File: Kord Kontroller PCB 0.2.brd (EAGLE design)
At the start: 242.5 x 100 mm, 190 parts, among them IC2 74HCT1G125DBV, J1 MIDIOUTB, J2 MIDIOUTA, J3 FTSH-105-01-L-DV-KJ, SW2 SPST_TACT-KMR2, U1 AP2112K-3.3, U2 ATSAMD51J19A-AUT, Y1 ECS-.327-12.5-17X-TR

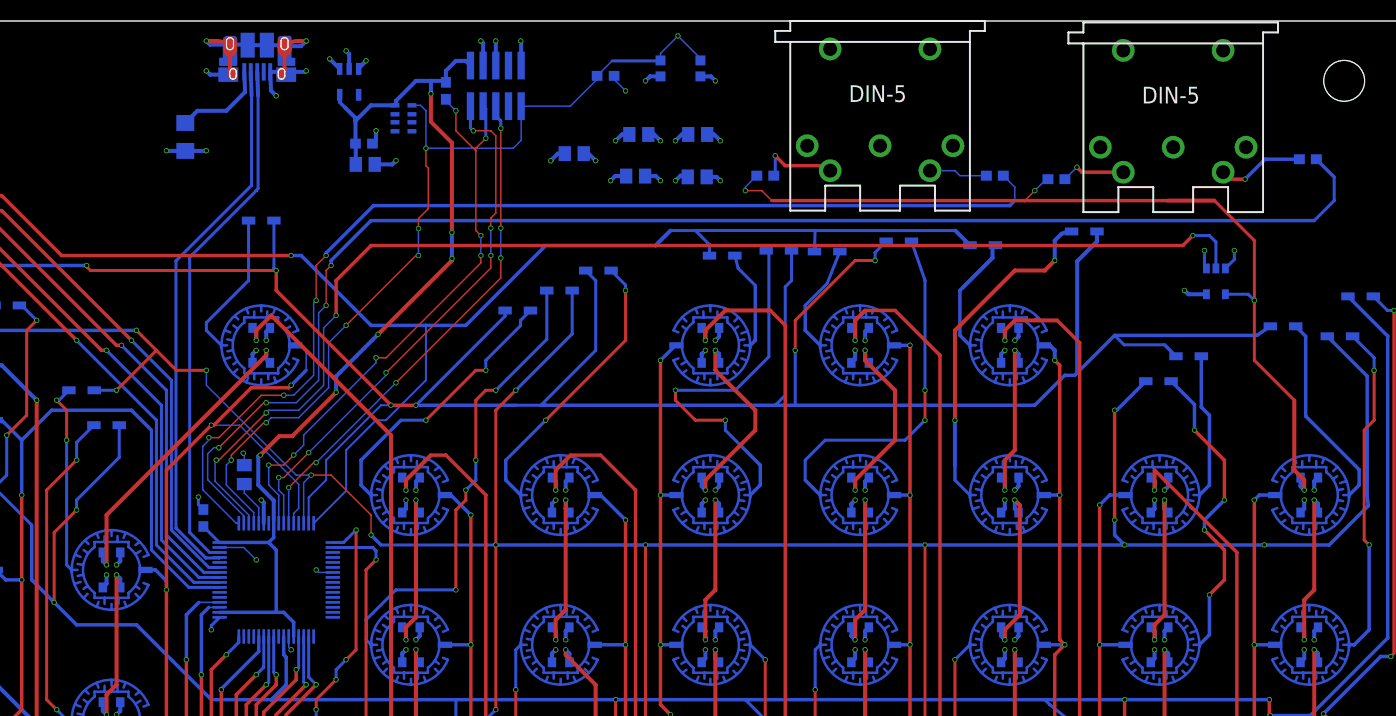
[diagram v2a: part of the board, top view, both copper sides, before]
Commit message: Rerouted, gave better routes, switched voltage shifter part
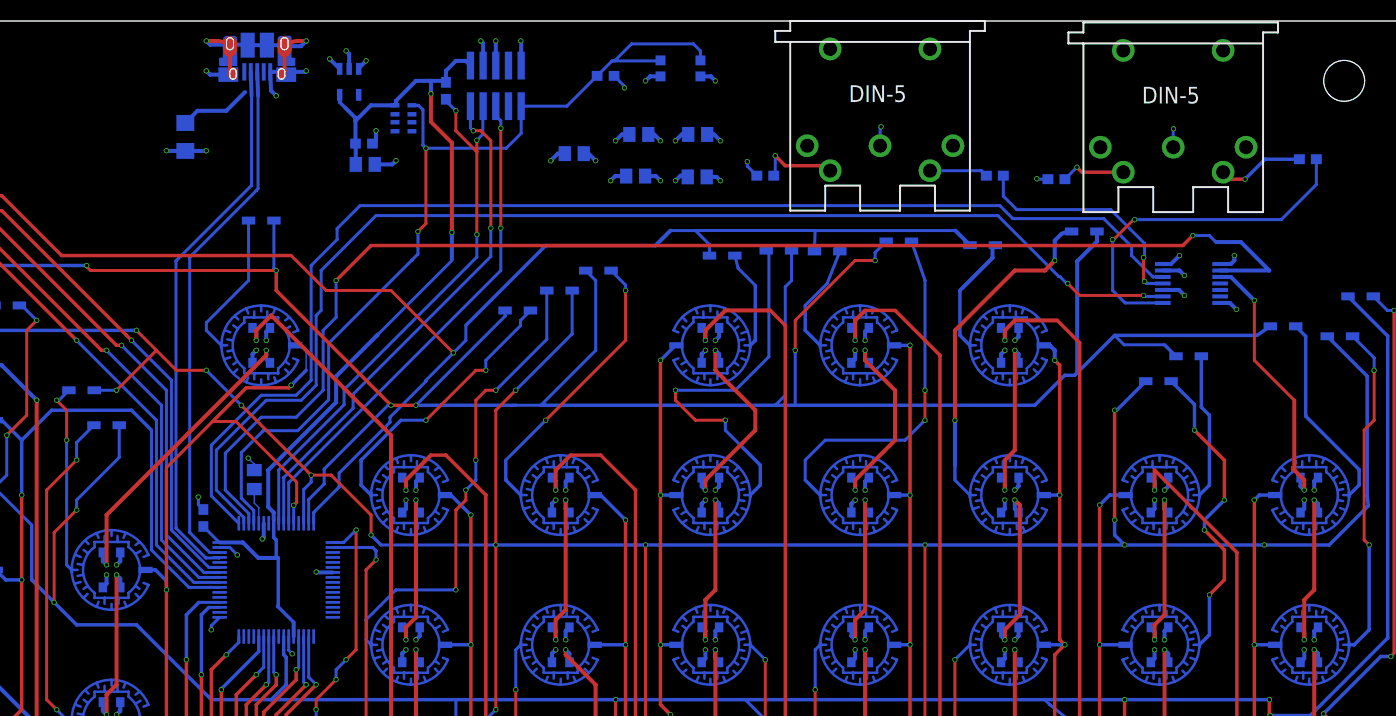
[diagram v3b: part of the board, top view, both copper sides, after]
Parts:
- removed IC2: 74HCT1G125DBV, 74xx-little-us:SOT23-5
- added U3: SN74LV4T125PWR, SN74LV4T125PWR:SOP65P640X120-14N
- moved C1 1.12 mm to (126.8, 54.0)
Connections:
- net N$66 renamed VBUS
- removed net MIDIOUTA: R4.1, U2.50
- removed net MIDIOUTB: R6.1, U2.49
- new net MIDIOUTA_3V: U2.50, U3.9
- new net MIDIOUTA_5V: R4.1, U3.8
- new net MIDIOUTB_3V: U2.49, U3.12
- new net MIDIOUTB_5V: R6.1, U3.11
- net GND: now also U3.1, U3.10, U3.13, U3.7; no longer IC2.1, IC2.3
- net LEVELSHIFT_3V: now also U3.2; no longer IC2.2
- net LEVELSHIFT_5V: now also U3.3; no longer IC2.4, R3.1, R5.1
- net VDD: now also R3.1, R5.1, U3.14; no longer IC2.5
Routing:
- net MIDIOUTA: track 143.1 -> 0.00 mm, vias 4 -> 0
- net MIDIOUTB_3V: track 0.00 -> 125.1 mm
- net MIDIOUTA_3V: track 0.00 -> 122.8 mm, vias 0 -> 2
- net MIDIOUTB: track 110.5 -> 0.00 mm, vias 4 -> 0
- net LEVELSHIFT_5V: track 89.9 -> 26.9 mm, vias 4 -> 2
- net MIDIOUTA_5V: track 0.00 -> 35.9 mm, vias 0 -> 2
- net MIDIOUTB_5V: track 0.00 -> 24.0 mm, vias 0 -> 2
- net LEVELSHIFT_3V: track 125.7 -> 133.7 mm, vias 4 -> 2
- net 3.3V: track 103.7 -> 97.0 mm, vias 6 -> 2
- net GND: track 153.0 -> 159.2 mm, vias 84 -> 88
- net SWDCLK: track 59.6 -> 56.9 mm, vias 7 -> 3
- net VDD: track 92.7 -> 95.3 mm, vias 64 -> 66
- net NRESET: track 90.4 -> 92.8 mm, vias 7 -> 2
- net VBUS: track 9.30 -> 7.27 mm
- net SWDIO: track 53.4 -> 51.7 mm, vias 6 -> 2
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
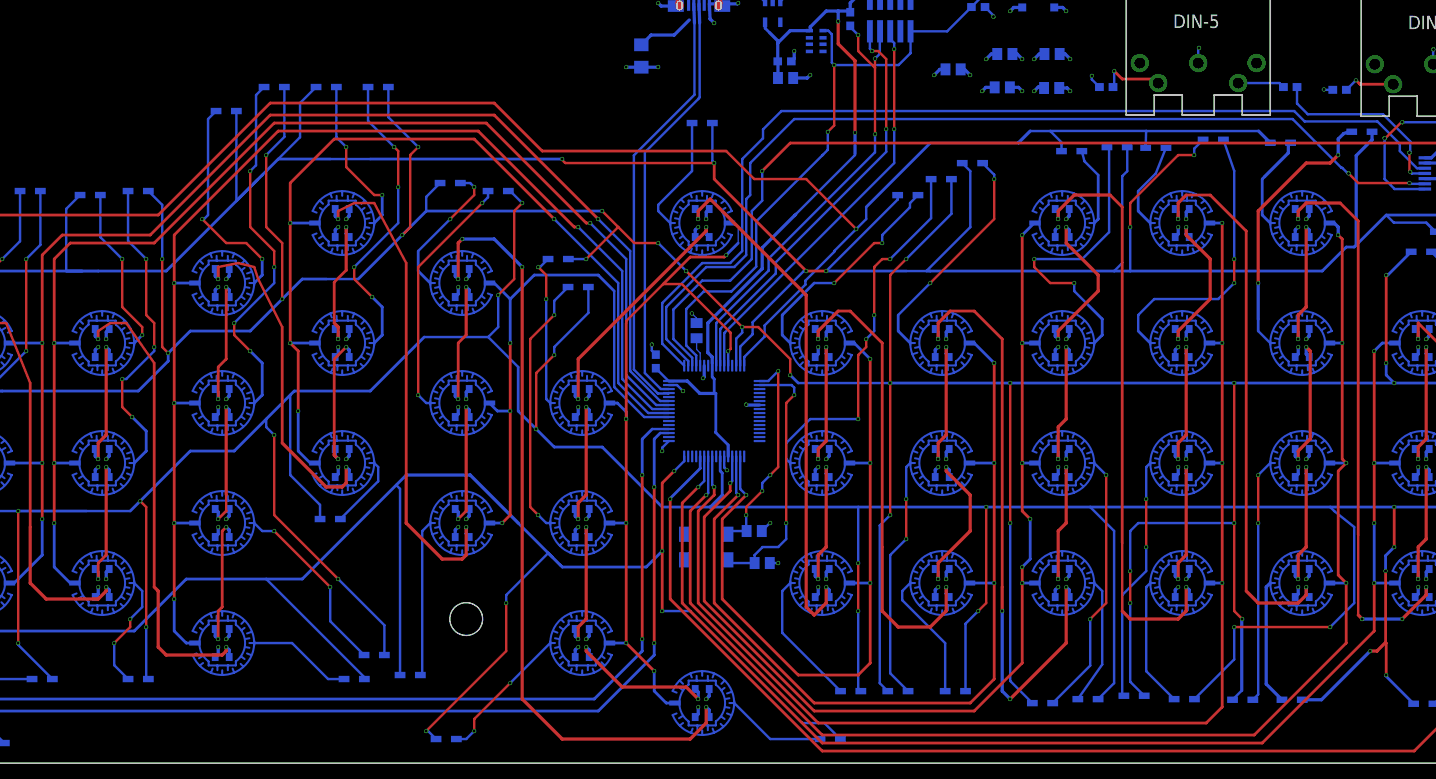
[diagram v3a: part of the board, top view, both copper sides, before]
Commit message: Moved caps
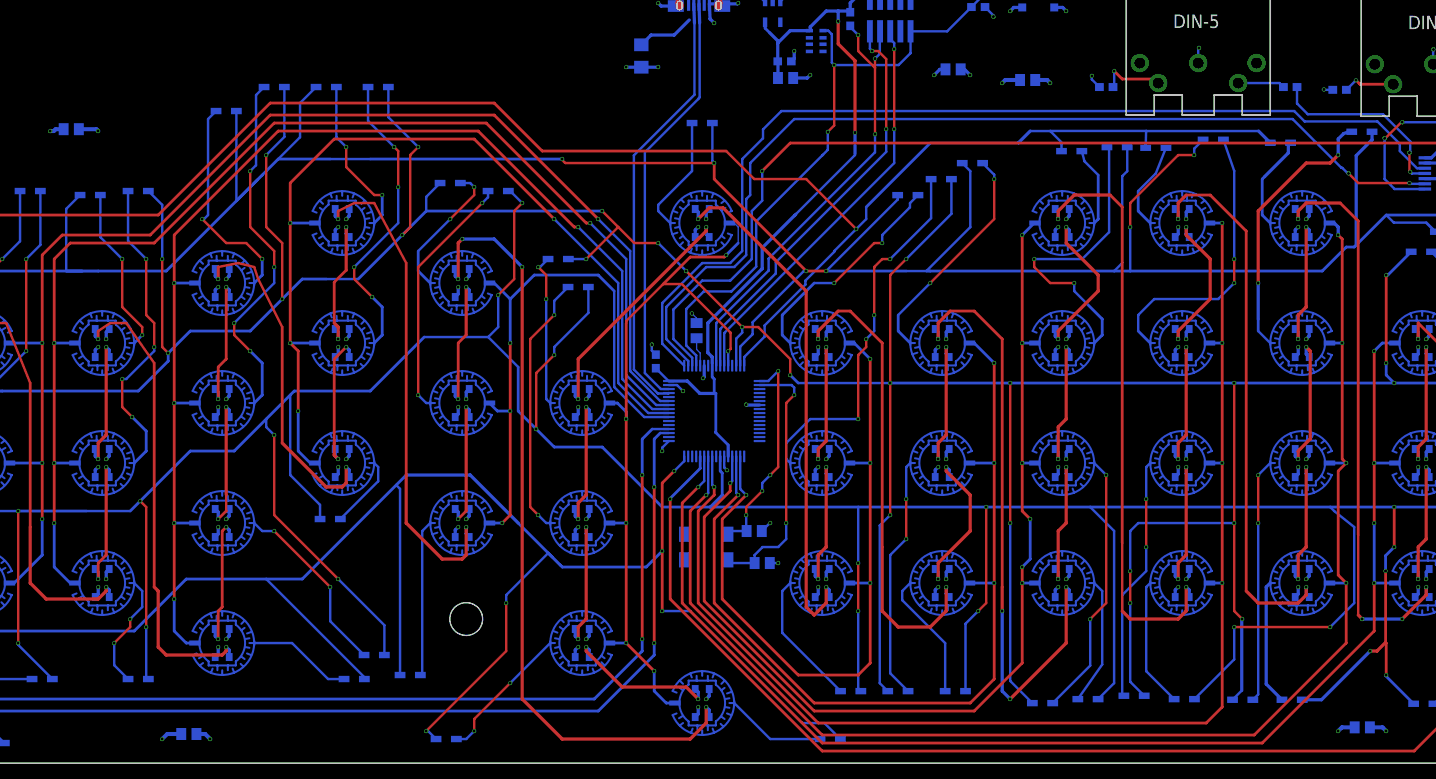
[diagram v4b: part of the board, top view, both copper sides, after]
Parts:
- moved C4 132.8 mm to (63.3, 3.63)
- moved C3 123.0 mm to (48.6, 79.2)
- moved C6 91.8 mm to (210.0, 4.46)
- moved C5 3.16 mm to (168.2, 85.4)
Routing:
- net VDD: track 95.3 -> 97.9 mm
- net GND: track 159.2 -> 161.6 mm
- net N$40: track 67.4 -> 66.2 mm
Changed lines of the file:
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@@
 <?xml version="1.0" encoding="utf-8"?>
 <!DOCTYPE eagle SYSTEM "eagle.dtd">
-<eagle version="9.2.2">
+<eagle version="9.4.2">
 <drawing>
 <settings>
@@
 <setting verticaltext="up"/>
 </settings>
-<grid distance="10" unitdist="mm" unit="mm" style="lines" multiple="1" display="yes" altdistance="1" altunitdist="mm" altunit="mm"/>
+<grid distance="1" unitdist="mm" unit="mm" style="lines" multiple="1" display="yes" altdistance="1" altunitdist="mm" altunit="mm"/>
 <layers>
 <layer number="1" name="Top" color="4" fill="1" visible="yes" active="yes"/>
@@
 <attribute name="VALUE" x="139.952" y="86.392" size="0.4064" layer="28" ratio="10" rot="MR180"/>
 </element>
-<element name="C3" library="microbuilder" package="0805-NO" value="10u" x="171.23" y="88.63" smashed="yes" rot="MR0">
-<attribute name="NAME" x="169.198" y="88.503" size="0.8128" layer="26" ratio="18" rot="MR0"/>
-<attribute name="VALUE" x="169.198" y="87.868" size="0.4064" layer="28" ratio="10" rot="MR0"/>
-</element>
-<element name="C4" library="microbuilder" package="0805-NO" value="10u" x="165.33" y="88.63" smashed="yes" rot="MR0">
-<attribute name="NAME" x="163.298" y="88.503" size="0.8128" layer="26" ratio="18" rot="MR0"/>
-<attribute name="VALUE" x="163.298" y="87.868" size="0.4064" layer="28" ratio="10" rot="MR0"/>
-</element>
-<element name="C5" library="microbuilder" package="0805-NO" value="10u" x="171.18" y="84.38" smashed="yes" rot="MR0">
-<attribute name="NAME" x="169.148" y="84.253" size="0.8128" layer="26" ratio="18" rot="MR0"/>
-<attribute name="VALUE" x="169.148" y="83.618" size="0.4064" layer="28" ratio="10" rot="MR0"/>
-</element>
-<element name="C6" library="microbuilder" package="0805-NO" value="10u" x="165.01" y="84.46" smashed="yes" rot="MR0">
-<attribute name="NAME" x="162.978" y="84.333" size="0.8128" layer="26" ratio="18" rot="MR0"/>
-<attribute name="VALUE" x="162.978" y="83.698" size="0.4064" layer="28" ratio="10" rot="MR0"/>
+<element name="C3" library="microbuilder" package="0805-NO" value="10u" x="48.63" y="79.23" smashed="yes" rot="MR0">
+<attribute name="NAME" x="46.598" y="79.103" size="0.8128" layer="26" ratio="18" rot="MR0"/>
+<attribute name="VALUE" x="46.598" y="78.468" size="0.4064" layer="28" ratio="10" rot="MR0"/>
+</element>
+<element name="C4" library="microbuilder" package="0805-NO" value="10u" x="63.33" y="3.63" smashed="yes" rot="MR0">
+<attribute name="NAME" x="61.298" y="3.503" size="0.8128" layer="26" ratio="18" rot="MR0"/>
+<attribute name="VALUE" x="61.298" y="2.868" size="0.4064" layer="28" ratio="10" rot="MR0"/>
+</element>
+<element name="C5" library="microbuilder" package="0805-NO" value="10u" x="168.18" y="85.38" smashed="yes" rot="MR0">
+<attribute name="NAME" x="166.148" y="85.253" size="0.8128" layer="26" ratio="18" rot="MR0"/>
+<attribute name="VALUE" x="166.148" y="84.618" size="0.4064" layer="28" ratio="10" rot="MR0"/>
+</element>
+<element name="C6" library="microbuilder" package="0805-NO" value="10u" x="210.01" y="4.46" smashed="yes" rot="MR0">
+<attribute name="NAME" x="207.978" y="4.333" size="0.8128" layer="26" ratio="18" rot="MR0"/>
+<attribute name="VALUE" x="207.978" y="3.698" size="0.4064" layer="28" ratio="10" rot="MR0"/>
 </element>
 <element name="C9" library="microbuilder" package="0805-NO" value="10µF" x="158.86" y="86.71" smashed="yes" rot="MR0">
@@
 <wire x1="153.54" y1="97.96" x2="153.5" y2="98" width="0.4064" layer="16"/>
 <via x="153.5" y="98" extent="1-16" drill="0.35"/>
-<wire x1="172.18" y1="88.63" x2="172.87" y2="88.63" width="0.4064" layer="16"/>
-<wire x1="172.87" y1="88.63" x2="173.5" y2="88" width="0.4064" layer="16"/>
-<via x="173.5" y="88" extent="1-16" drill="0.35"/>
-<wire x1="172.13" y1="84.38" x2="173.12" y2="84.38" width="0.4064" layer="16"/>
-<wire x1="173.12" y1="84.38" x2="173.5" y2="84" width="0.4064" layer="16"/>
-<via x="173.5" y="84" extent="1-16" drill="0.35"/>
-<wire x1="166.28" y1="88.63" x2="166.87" y2="88.63" width="0.4064" layer="16"/>
-<wire x1="166.87" y1="88.63" x2="167.5" y2="88" width="0.4064" layer="16"/>
-<via x="167.5" y="88" extent="1-16" drill="0.35"/>
-<wire x1="165.96" y1="84.46" x2="167.04" y2="84.46" width="0.4064" layer="16"/>
-<wire x1="167.04" y1="84.46" x2="167.5" y2="84" width="0.4064" layer="16"/>
-<via x="167.5" y="84" extent="1-16" drill="0.35"/>
 <wire x1="157.91" y1="86.71" x2="157.21" y2="86.71" width="0.4064" layer="16"/>
 <wire x1="157.21" y1="86.71" x2="156.5" y2="86" width="0.4064" layer="16"/>
@@
 <wire x1="189.5" y1="89.3" x2="189.6" y2="89.4" width="0.3048" layer="16"/>
 <via x="189.6" y="89.4" extent="1-16" drill="0.35"/>
+<wire x1="49.58" y1="79.23" x2="51.77" y2="79.23" width="0.508" layer="16"/>
+<wire x1="51.77" y1="79.23" x2="52" y2="79" width="0.508" layer="16"/>
+<via x="52" y="79" extent="1-16" drill="0.35"/>
+<wire x1="64.28" y1="3.63" x2="65.37" y2="3.63" width="0.508" layer="16"/>
+<wire x1="65.37" y1="3.63" x2="66" y2="3" width="0.508" layer="16"/>
+<via x="66" y="3" extent="1-16" drill="0.35"/>
+<wire x1="210.96" y1="4.46" x2="212.54" y2="4.46" width="0.508" layer="16"/>
+<wire x1="212.54" y1="4.46" x2="213" y2="4" width="0.508" layer="16"/>
+<via x="213" y="4" extent="1-16" drill="0.35"/>
+<wire x1="169.13" y1="85.38" x2="170.62" y2="85.38" width="0.508" layer="16"/>
+<wire x1="170.62" y1="85.38" x2="171" y2="85" width="0.508" layer="16"/>
+<via x="171" y="85" extent="1-16" drill="0.35"/>
 </signal>
 <signal name="ROW1">
@@
 <vertex x="243" y="0"/>
 </polygon>
-<wire x1="170.28" y1="88.63" x2="169.63" y2="88.63" width="0.4064" layer="16"/>
-<wire x1="169.63" y1="88.63" x2="169" y2="88" width="0.4064" layer="16"/>
-<via x="169" y="88" extent="1-16" drill="0.35"/>
-<wire x1="169.5" y1="84.5" x2="170.11" y2="84.5" width="0.4064" layer="16"/>
-<wire x1="170.23" y1="84.38" x2="170.11" y2="84.5" width="0.4064" layer="16"/>
-<wire x1="169.5" y1="84.5" x2="169" y2="84" width="0.4064" layer="16"/>
-<via x="169" y="84" extent="1-16" drill="0.35"/>
-<wire x1="163.63" y1="88.63" x2="164.38" y2="88.63" width="0.4064" layer="16"/>
-<wire x1="163.63" y1="88.63" x2="163" y2="88" width="0.4064" layer="16"/>
-<via x="163" y="88" extent="1-16" drill="0.35"/>
-<wire x1="164.06" y1="84.46" x2="162.96" y2="84.46" width="0.4064" layer="16"/>
-<wire x1="162.96" y1="84.46" x2="162.5" y2="84" width="0.4064" layer="16"/>
-<via x="162.5" y="84" extent="1-16" drill="0.35"/>
 <wire x1="159.81" y1="86.71" x2="160.29" y2="86.71" width="0.4064" layer="16"/>
 <wire x1="160.29" y1="86.71" x2="161" y2="86" width="0.4064" layer="16"/>
@@
 <wire x1="205.25" y1="84.15" x2="205.2" y2="84.2" width="0.3048" layer="16"/>
 <via x="205.2" y="84.2" extent="1-16" drill="0.35"/>
+<wire x1="46.68" y1="79.23" x2="46.45" y2="79" width="0.508" layer="16"/>
+<wire x1="46" y1="79" x2="46.45" y2="79" width="0.508" layer="16"/>
+<wire x1="47.68" y1="79.23" x2="46.68" y2="79.23" width="0.508" layer="16"/>
+<via x="46" y="79" extent="1-16" drill="0.35"/>
+<wire x1="62.38" y1="3.63" x2="60.63" y2="3.63" width="0.508" layer="16"/>
+<wire x1="60.63" y1="3.63" x2="60" y2="3" width="0.508" layer="16"/>
+<via x="60" y="3" extent="1-16" drill="0.35"/>
+<wire x1="209.06" y1="4.46" x2="207.46" y2="4.46" width="0.508" layer="16"/>
+<wire x1="207.46" y1="4.46" x2="207" y2="4" width="0.508" layer="16"/>
+<via x="207" y="4" extent="1-16" drill="0.35"/>
+<wire x1="167.23" y1="85.38" x2="165.38" y2="85.38" width="0.508" layer="16"/>
+<wire x1="165.38" y1="85.38" x2="165" y2="85" width="0.508" layer="16"/>
+<via x="165" y="85" extent="1-16" drill="0.35"/>
 </signal>
 <signal name="D+">
@@
 <contactref element="LED25" pad="1"/>
 <contactref element="LED24" pad="3"/>
-<wire x1="128.5" y1="70.5" x2="140.5" y2="58.5" width="0.4064" layer="1"/>
-<wire x1="128.5" y1="70.5" x2="127" y2="69" width="0.4064" layer="1"/>
-<wire x1="127" y1="68" x2="127" y2="69" width="0.4064" layer="1"/>
+<wire x1="130.1" y1="69.4" x2="140.5" y2="59" width="0.4064" layer="1"/>
+<wire x1="127" y1="68" x2="128.4" y2="69.4" width="0.4064" layer="1"/>
+<wire x1="130.1" y1="69.4" x2="128.4" y2="69.4" width="0.4064" layer="1"/>
 <via x="127" y="68" extent="1-16" drill="0.35"/>
 <wire x1="126.625" y1="69.25" x2="127" y2="68.875" width="0.4064" layer="16"/>
@@
 <wire x1="143" y1="22" x2="143.375" y2="21.625" width="0.4064" layer="16"/>
 <wire x1="143.375" y1="21.625" x2="143.375" y2="20.75" width="0.4064" layer="16"/>
-<wire x1="140.5" y1="58.5" x2="140.5" y2="19.5" width="0.4064" layer="1"/>
+<wire x1="140.5" y1="59" x2="140.5" y2="19.5" width="0.4064" layer="1"/>
 </signal>
 <signal name="N$41">
